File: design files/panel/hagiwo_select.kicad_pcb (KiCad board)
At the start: 2 copper layers, 29.9 x 128.4 mm, 4 parts

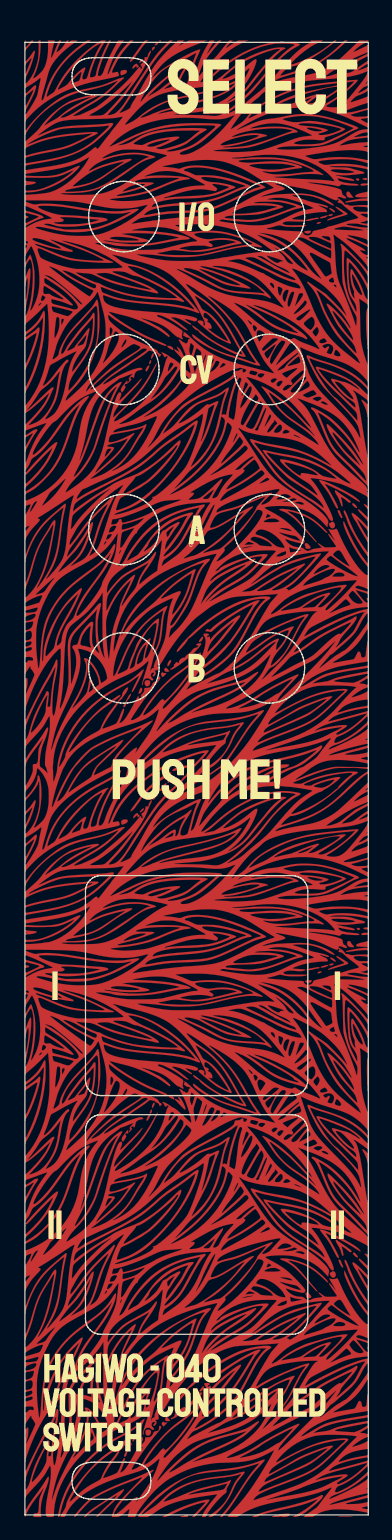
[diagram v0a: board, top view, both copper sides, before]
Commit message: v2 pcb and panel, since jlc complained because of cutout dimensions
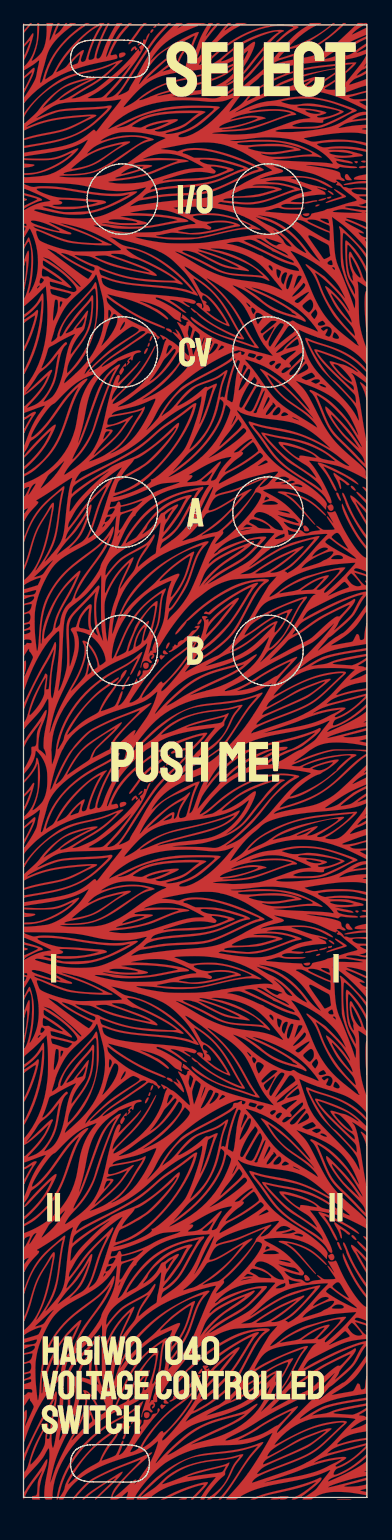
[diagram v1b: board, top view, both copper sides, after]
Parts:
- removed the G*** at (16.1, 66.4) (x4)
- added G*** (x4): LOGO, LOGO, F.Cu at (16.0, 64.9)
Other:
- outline, holes or cut-outs redrawn

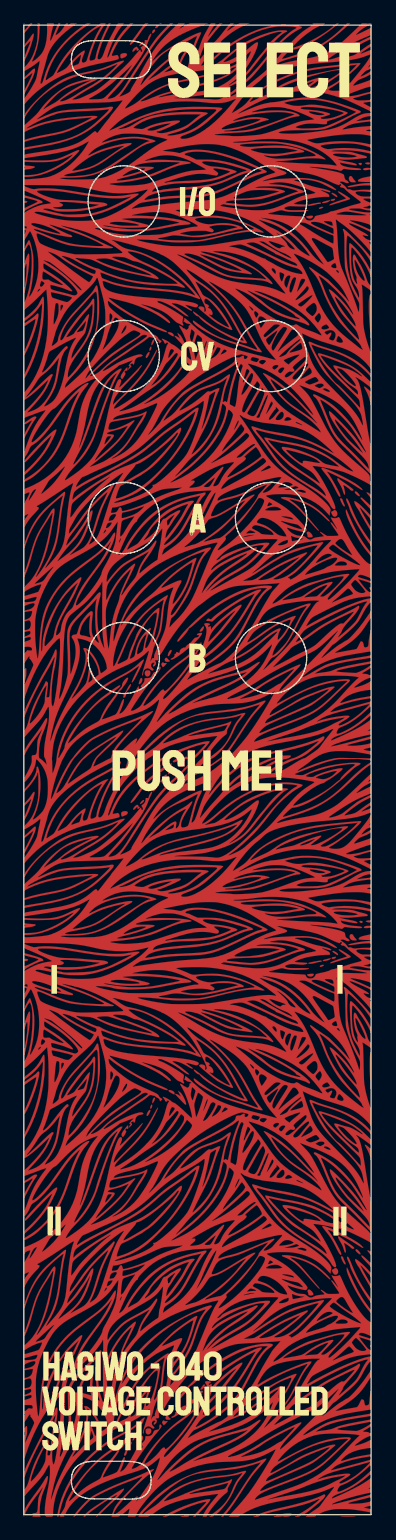
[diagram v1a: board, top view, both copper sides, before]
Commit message: fixed an error with the panel pcb gerber
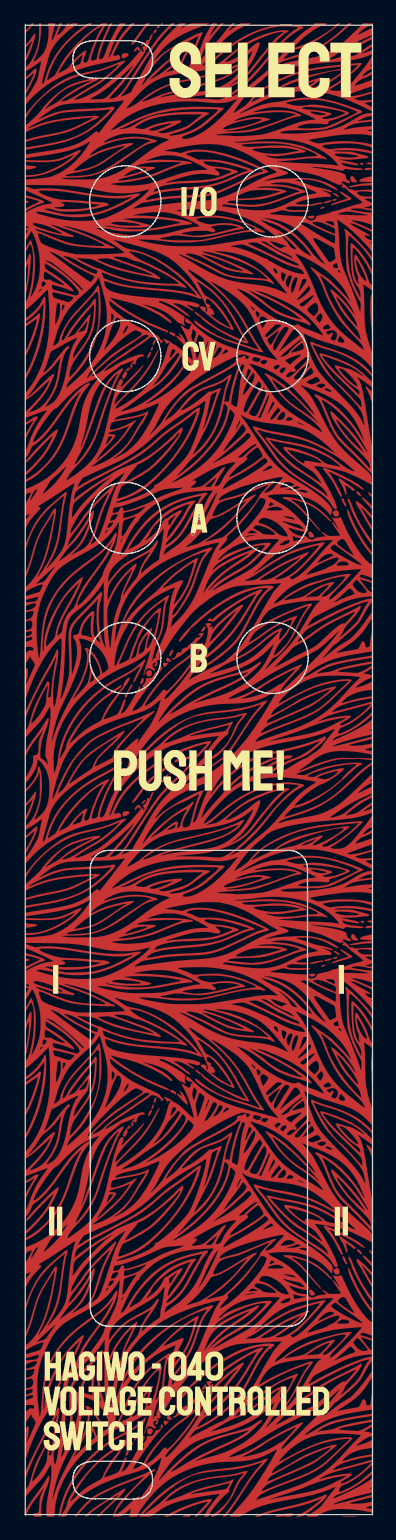
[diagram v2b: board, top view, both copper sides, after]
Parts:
- removed the G*** at (16.0, 64.9) (x4)
- added G*** (x4): LOGO, LOGO, F.Cu at (16.1, 64.9)
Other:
- outline, holes or cut-outs redrawn

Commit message: v4 better spacing
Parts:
- removed the G*** at (16.1, 64.9) (x4)
- added G*** (x4): LOGO, LOGO, F.Cu at (0.00, 0.00)
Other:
- board size 29.9 x 128.4 mm -> 4232.1 x 3677.3 mm

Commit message: fixed botched kicad export
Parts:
- removed the G*** at (0.00, 0.00) (x4)
- added G*** (x4): LOGO, LOGO, F.Cu at (18.0, 67.9)
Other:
- board size 4232.1 x 3677.3 mm -> 30 x 128.4 mm
- net class Default removed
